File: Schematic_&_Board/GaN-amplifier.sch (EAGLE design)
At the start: 49 parts, among them IC1 LT3080, Q1 MMBT3906LT1SMD, T1 IRL3714S, T2 IRL3714S, T3 IRL3714S, U1 TPS7A30XX, U2 HMC1099, U3 LT1783, U4 CPC1117NTR, U5 LT1783, U6 LTC2924, U7 LCA701S, X1 SMA-142-0701-801/806, X2 SMA-142-0701-801/806

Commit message: Quick Sync to talk sequencing with AR
A few more updates to discuss.

DSB
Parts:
- added R16: 1k, jqi_passives:R_SMDR0603
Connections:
- new net N$14: R16.2, T3.S
- new net N$16: R16.1, U4.P$1
- net +5V: now also T3.D
- net -8V: now also U4.P$4
- net GND: now also U4.P$2
- net VGG_EN: now also T3.G
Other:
- moved on the sheet: T3, U4
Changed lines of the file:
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@@
 <part name="R14" library="jqi_passives" deviceset="R_SMD" device="R0603" value="2M"/>
 <part name="R15" library="jqi_passives" deviceset="R_SMD" device="R0603" value="54.9k"/>
+<part name="P+9" library="supply1" deviceset="+5V" device=""/>
+<part name="R16" library="jqi_passives" deviceset="R_SMD" device="R0603" value="1k"/>
+<part name="GND11" library="supply1" deviceset="GND" device=""/>
+<part name="SUPPLY2" library="supply2" deviceset="-8V" device=""/>
 </parts>
 <sheets>
@@
 <instance part="C16" gate="G$1" x="76.2" y="123.19"/>
 <instance part="R4" gate="G$1" x="85.09" y="123.19" rot="R90"/>
-<instance part="U4" gate="G$1" x="76.2" y="218.44"/>
+<instance part="U4" gate="G$1" x="200.66" y="128.27"/>
 <instance part="Q1" gate="G$1" x="34.29" y="66.04" rot="MR180"/>
 <instance part="R5" gate="G$1" x="31.75" y="83.82" rot="R90"/>
@@
 <instance part="R12" gate="G$1" x="59.69" y="71.12" rot="R180"/>
 <instance part="GND9" gate="1" x="100.33" y="57.15"/>
-<instance part="T3" gate="G$1" x="90.17" y="236.22"/>
+<instance part="T3" gate="G$1" x="170.18" y="130.81" rot="R90"/>
 <instance part="U7" gate="G$1" x="133.35" y="124.46"/>
 <instance part="P+6" gate="1" x="93.98" y="135.89"/>
@@
 <instance part="R14" gate="G$1" x="143.51" y="110.49" rot="R270"/>
 <instance part="R15" gate="G$1" x="133.35" y="102.87"/>
+<instance part="P+9" gate="1" x="161.29" y="139.7"/>
+<instance part="R16" gate="G$1" x="184.15" y="133.35" rot="R180"/>
+<instance part="GND11" gate="1" x="190.5" y="114.3"/>
+<instance part="SUPPLY2" gate="G$1" x="212.09" y="139.7" rot="R180"/>
 </instances>
 <busses>
@@
 <junction x="123.19" y="102.87"/>
 </segment>
+<segment>
+<pinref part="U4" gate="G$1" pin="P$2"/>
+<pinref part="GND11" gate="1" pin="GND"/>
+<wire x1="193.04" y1="123.19" x2="190.5" y2="123.19" width="0.1524" layer="91"/>
+<wire x1="190.5" y1="123.19" x2="190.5" y2="116.84" width="0.1524" layer="91"/>
+</segment>
 </net>
 <net name="N$15" class="0">
@@
 <wire x1="93.98" y1="133.35" x2="93.98" y2="129.54" width="0.1524" layer="91"/>
 <wire x1="93.98" y1="129.54" x2="97.79" y2="129.54" width="0.1524" layer="91"/>
+</segment>
+<segment>
+<pinref part="P+9" gate="1" pin="+5V"/>
+<pinref part="T3" gate="G$1" pin="D"/>
+<wire x1="161.29" y1="137.16" x2="161.29" y2="133.35" width="0.1524" layer="91"/>
+<wire x1="161.29" y1="133.35" x2="165.1" y2="133.35" width="0.1524" layer="91"/>
 </segment>
 </net>
@@
 <junction x="119.38" y="91.44"/>
 </segment>
+<segment>
+<pinref part="SUPPLY2" gate="G$1" pin="-8V"/>
+<pinref part="U4" gate="G$1" pin="P$4"/>
+<wire x1="212.09" y1="137.16" x2="212.09" y2="133.35" width="0.1524" layer="91"/>
+<wire x1="212.09" y1="133.35" x2="208.28" y2="133.35" width="0.1524" layer="91"/>
+</segment>
 </net>
 <net name="VPIN_DET" class="0">
@@
 <wire x1="8.89" y1="120.65" x2="1.27" y2="120.65" width="0.1524" layer="91"/>
 <label x="0" y="120.65" size="1.778" layer="95"/>
+</segment>
+<segment>
+<pinref part="T3" gate="G$1" pin="G"/>
+<wire x1="172.72" y1="128.27" x2="172.72" y2="119.38" width="0.1524" layer="91"/>
+<label x="172.72" y="118.11" size="1.778" layer="95" rot="R90"/>
 </segment>
 </net>
@@
 </segment>
 </net>
+<net name="N$14" class="0">
+<segment>
+<pinref part="T3" gate="G$1" pin="S"/>
+<pinref part="R16" gate="G$1" pin="2"/>
+<wire x1="175.26" y1="133.35" x2="179.07" y2="133.35" width="0.1524" layer="91"/>
+</segment>
+</net>
+<net name="N$16" class="0">
+<segment>
+<pinref part="R16" gate="G$1" pin="1"/>
+<pinref part="U4" gate="G$1" pin="P$1"/>
+<wire x1="189.23" y1="133.35" x2="193.04" y2="133.35" width="0.1524" layer="91"/>
+</segment>
+</net>

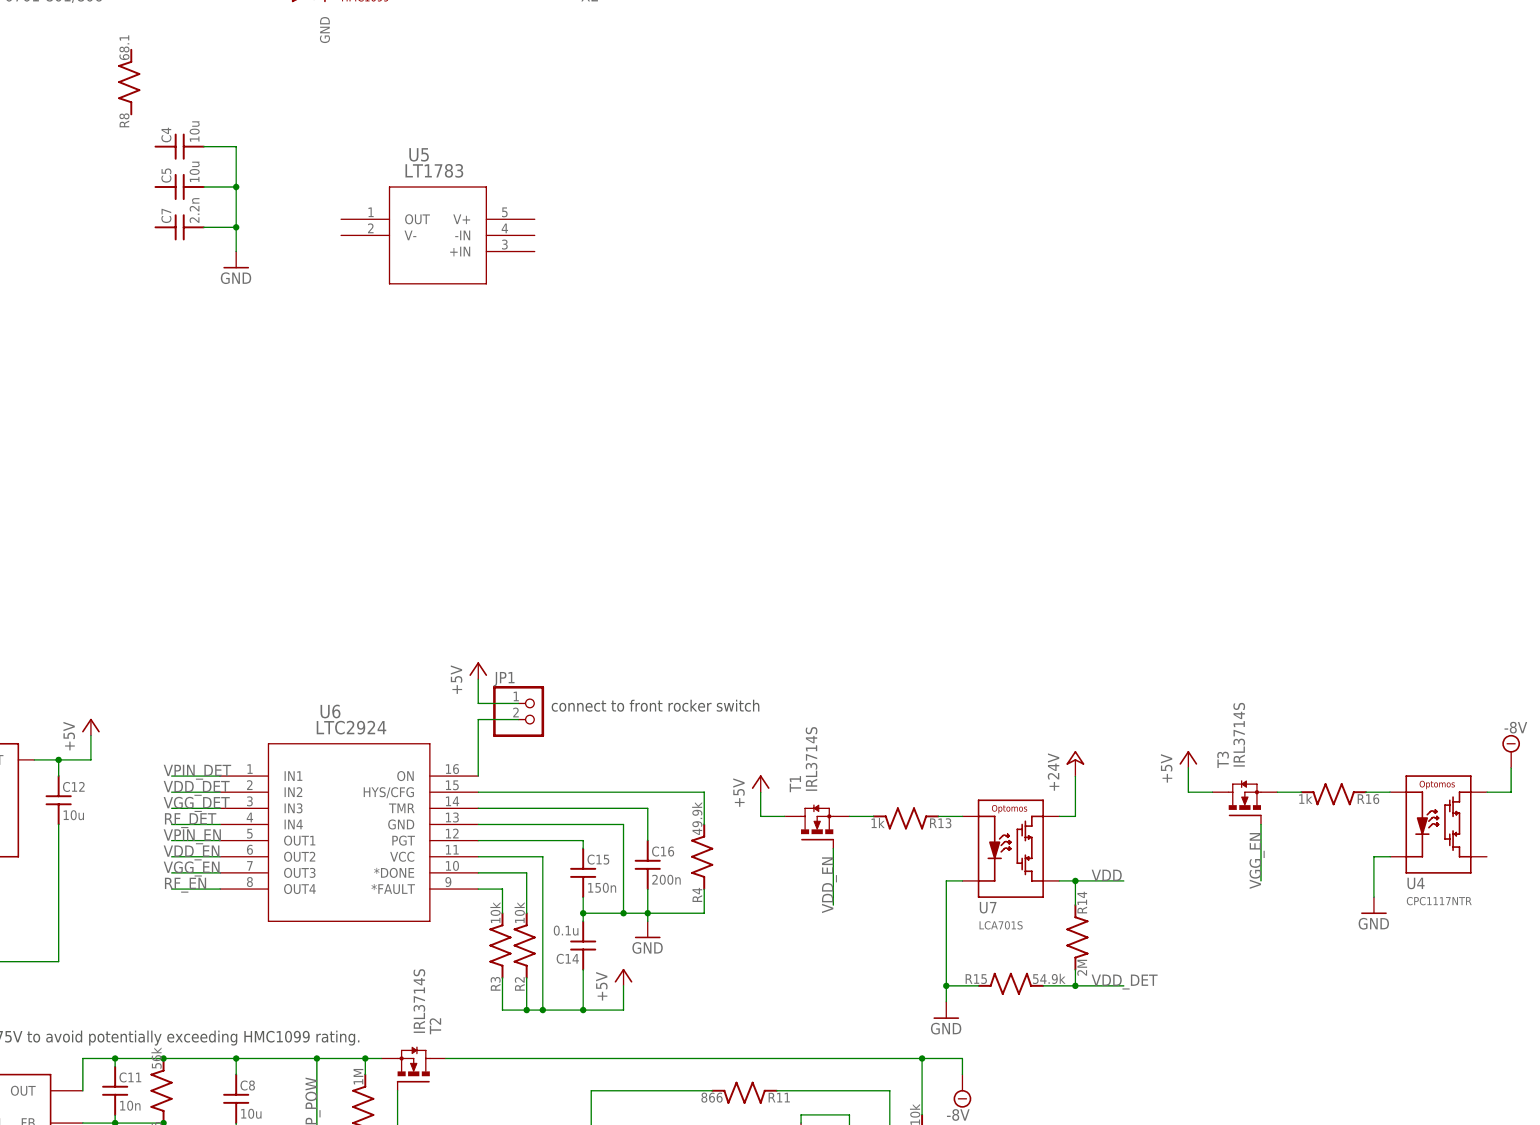
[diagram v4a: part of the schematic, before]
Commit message: Starting Vgg Control
Started setting up the power sequencing and setpoint control for the
amplifier gate voltage.

DSB
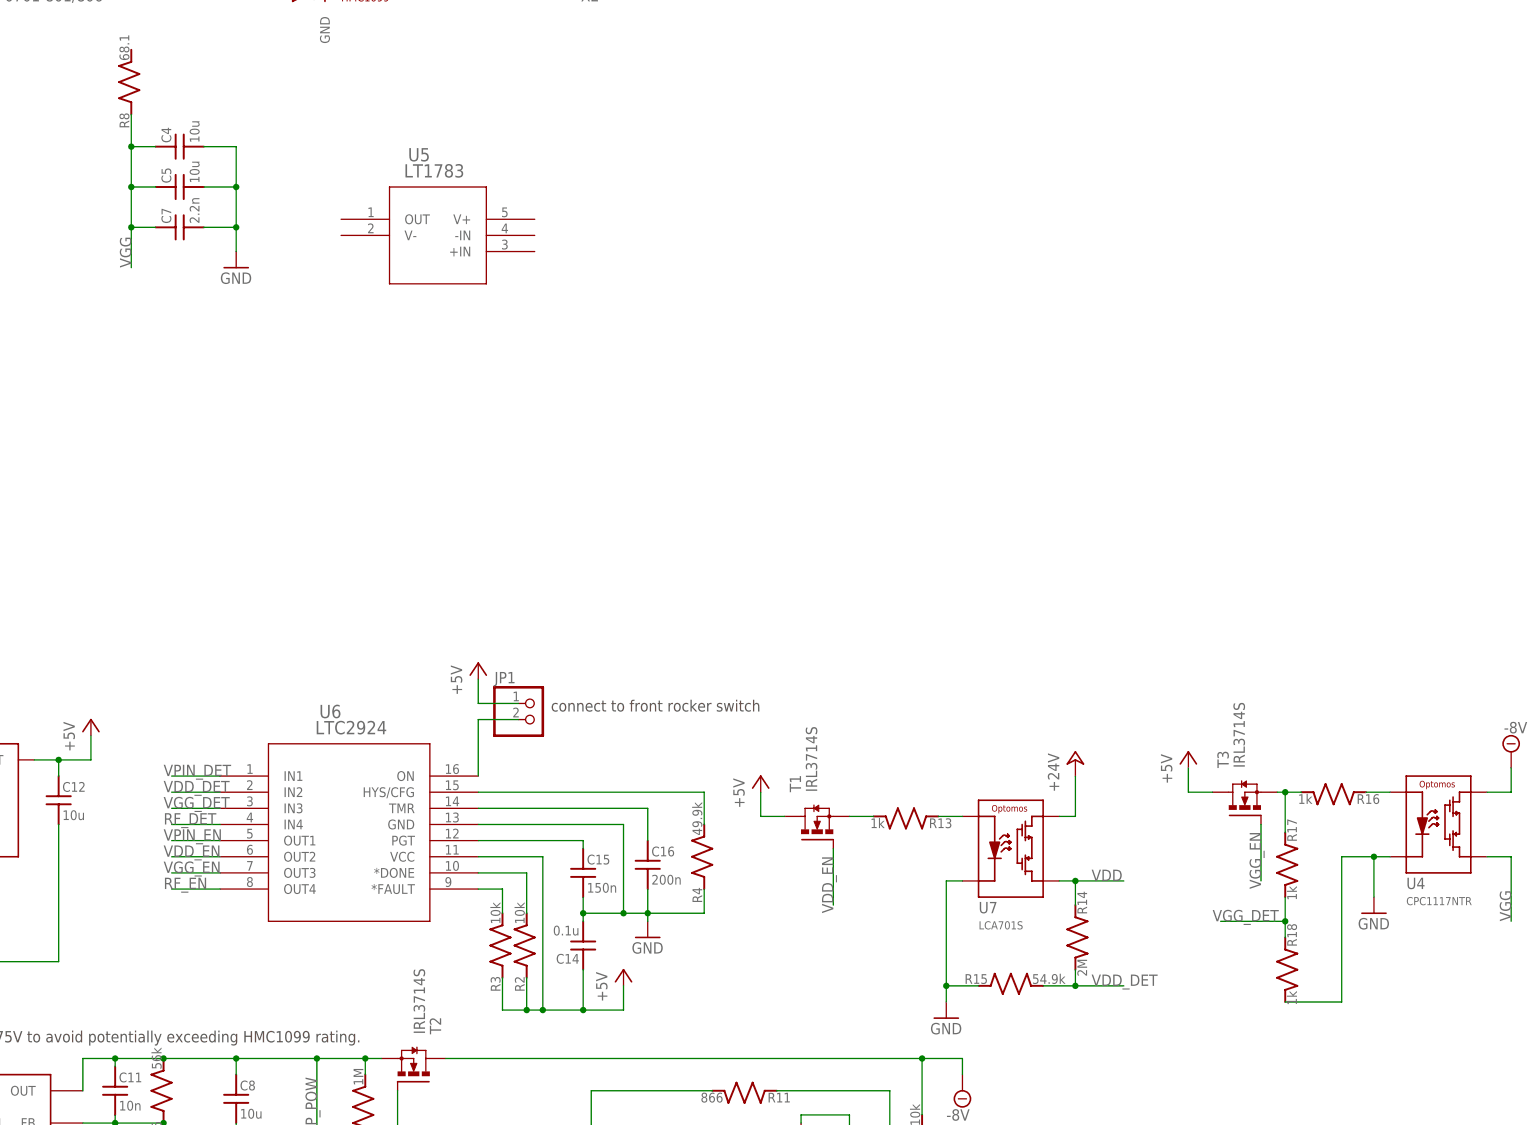
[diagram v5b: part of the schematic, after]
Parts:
- added R17, R18: 1k, jqi_passives:R_SMDR0603
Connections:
- new net VGG: C4.1, C5.1, C7.1, R8.1, U4.P$3
- net GND: now also R18.2
- net N$14: now also R17.1
- net VGG_DET: now also R17.2, R18.1
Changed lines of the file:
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@@
 <part name="GND11" library="supply1" deviceset="GND" device=""/>
 <part name="SUPPLY2" library="supply2" deviceset="-8V" device=""/>
+<part name="R17" library="jqi_passives" deviceset="R_SMD" device="R0603" value="1k"/>
+<part name="R18" library="jqi_passives" deviceset="R_SMD" device="R0603" value="1k"/>
 </parts>
 <sheets>
@@
 <instance part="GND11" gate="1" x="190.5" y="114.3"/>
 <instance part="SUPPLY2" gate="G$1" x="212.09" y="139.7" rot="R180"/>
+<instance part="R17" gate="G$1" x="176.53" y="121.92" rot="R270"/>
+<instance part="R18" gate="G$1" x="176.53" y="105.41" rot="R270"/>
 </instances>
 <busses>
@@
 <wire x1="193.04" y1="123.19" x2="190.5" y2="123.19" width="0.1524" layer="91"/>
 <wire x1="190.5" y1="123.19" x2="190.5" y2="116.84" width="0.1524" layer="91"/>
+<pinref part="R18" gate="G$1" pin="2"/>
+<wire x1="176.53" y1="100.33" x2="185.42" y2="100.33" width="0.1524" layer="91"/>
+<wire x1="185.42" y1="100.33" x2="185.42" y2="123.19" width="0.1524" layer="91"/>
+<wire x1="185.42" y1="123.19" x2="190.5" y2="123.19" width="0.1524" layer="91"/>
+<junction x="190.5" y="123.19"/>
 </segment>
 </net>
@@
 <label x="0" y="130.81" size="1.778" layer="95"/>
 </segment>
+<segment>
+<pinref part="R17" gate="G$1" pin="2"/>
+<pinref part="R18" gate="G$1" pin="1"/>
+<wire x1="176.53" y1="116.84" x2="176.53" y2="113.03" width="0.1524" layer="91"/>
+<wire x1="176.53" y1="113.03" x2="176.53" y2="110.49" width="0.1524" layer="91"/>
+<wire x1="176.53" y1="113.03" x2="166.37" y2="113.03" width="0.1524" layer="91"/>
+<junction x="176.53" y="113.03"/>
+<label x="165.1" y="113.03" size="1.778" layer="95"/>
+</segment>
 </net>
 <net name="RF_DET" class="0">
@@
 <pinref part="T3" gate="G$1" pin="S"/>
 <pinref part="R16" gate="G$1" pin="2"/>
-<wire x1="175.26" y1="133.35" x2="179.07" y2="133.35" width="0.1524" layer="91"/>
+<wire x1="175.26" y1="133.35" x2="176.53" y2="133.35" width="0.1524" layer="91"/>
+<pinref part="R17" gate="G$1" pin="1"/>
+<wire x1="176.53" y1="133.35" x2="179.07" y2="133.35" width="0.1524" layer="91"/>
+<wire x1="176.53" y1="127" x2="176.53" y2="133.35" width="0.1524" layer="91"/>
+<junction x="176.53" y="133.35"/>
 </segment>
 </net>
@@
 </segment>
 </net>
+<net name="VGG" class="0">
+<segment>
+<pinref part="U4" gate="G$1" pin="P$3"/>
+<wire x1="208.28" y1="123.19" x2="212.09" y2="123.19" width="0.1524" layer="91"/>
+<wire x1="212.09" y1="123.19" x2="212.09" y2="113.03" width="0.1524" layer="91"/>
+<label x="212.09" y="113.03" size="1.778" layer="95" rot="R90"/>
+</segment>
+<segment>
+<pinref part="C4" gate="G$1" pin="1"/>
+<pinref part="R8" gate="G$1" pin="1"/>
+<wire x1="-1.27" y1="234.95" x2="-5.08" y2="234.95" width="0.1524" layer="91"/>
+<wire x1="-5.08" y1="234.95" x2="-5.08" y2="240.03" width="0.1524" layer="91"/>
+<pinref part="C5" gate="G$1" pin="1"/>
+<wire x1="-1.27" y1="228.6" x2="-5.08" y2="228.6" width="0.1524" layer="91"/>
+<wire x1="-5.08" y1="228.6" x2="-5.08" y2="234.95" width="0.1524" layer="91"/>
+<junction x="-5.08" y="234.95"/>
+<pinref part="C7" gate="G$1" pin="1"/>
+<wire x1="-1.27" y1="222.25" x2="-5.08" y2="222.25" width="0.1524" layer="91"/>
+<wire x1="-5.08" y1="222.25" x2="-5.08" y2="228.6" width="0.1524" layer="91"/>
+<junction x="-5.08" y="228.6"/>
+<wire x1="-5.08" y1="222.25" x2="-5.08" y2="215.9" width="0.1524" layer="91"/>
+<junction x="-5.08" y="222.25"/>
+<label x="-5.08" y="215.9" size="1.778" layer="95" rot="R90"/>
+</segment>
+</net>
